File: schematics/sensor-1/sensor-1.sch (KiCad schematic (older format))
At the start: 12 parts, among them J1 Conn_01x06_Male, U1 SIC553-04, U2 SIC553-04, U3 SIC553-04

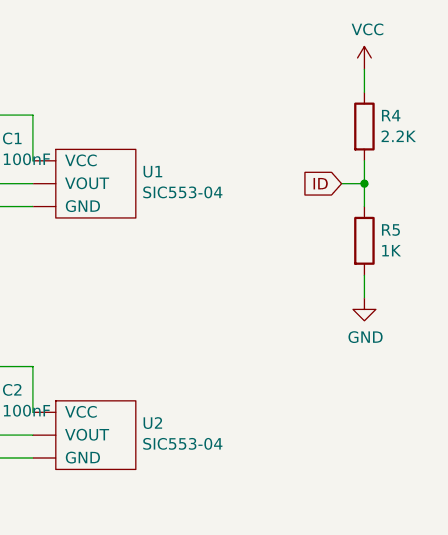
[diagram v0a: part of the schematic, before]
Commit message: Add sensor 2
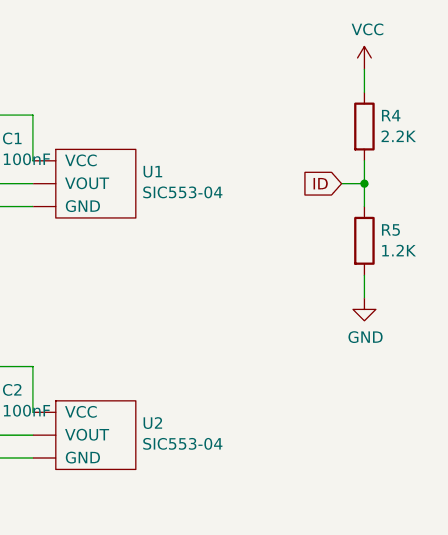
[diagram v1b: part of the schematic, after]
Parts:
- R5: value 1K -> 1.2K
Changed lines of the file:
@@
 P 5050 1650
 F 0 "R5" H 5120 1696 50  0000 L CNN
-F 1 "1K" H 5120 1605 50  0000 L CNN
+F 1 "1.2K" H 5120 1605 50  0000 L CNN
 F 2 "" V 4980 1650 50  0001 C CNN
 F 3 "~" H 5050 1650 50  0001 C CNN
